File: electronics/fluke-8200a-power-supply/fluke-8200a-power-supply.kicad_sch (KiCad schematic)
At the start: 77 parts, among them J10 Conn_01x01_Socket, J11 Conn_01x01_Socket, J12 Conn_01x01_Socket, J13 Conn_01x01_Socket, J14 Conn_01x01_Socket, J2 Conn_01x01_Socket, J3 Conn_01x01_Socket, J4 Conn_01x01_Socket, J5 Conn_01x01_Socket, J6 Conn_01x01_Socket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

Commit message: PCB work.
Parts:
- C1, C10, C11, C12, C13, C3, C4, C6, C7, C8, C9: symbol Device:C -> Device:C_Polarized
- C2: value 400 -> 400uF; symbol Device:C -> Device:C_Polarized
- C5: value 125 -> 125uF; symbol Device:C -> Device:C_Polarized
- Q13: Note (none) -> Actually uses 2N3391A
- renumbered Q8 to Q10
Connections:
- net +15V: now also C3.1; no longer C3.2
- net GND: now also C1.2; no longer C1.1
- net GNDS: now also C12.2, C2.2, C3.2, C4.1; no longer C12.1, C2.1, C3.1, C4.2
- net at R5.2, R7.1: now also C12.1; no longer C12.2
- net at D2.1 (K), D4.1 (K), R1.1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: now also C1.1; no longer C1.2
- net at D5.2 (A), D7.2 (A), R16.1: now also C4.2; no longer C4.1
- net at D6.1 (K), D8.1 (K), R6.1: now also C2.1; no longer C2.2
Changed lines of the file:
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@@
   (junction (at 40.64 81.28) (diameter 0) (color 0 0 0 0)
   )
+  (junction (at 82.55 168.91) (diameter 0) (color 0 0 0 0)
+  )
+  (junction (at 167.64 73.66) (diameter 0) (color 0 0 0 0)
+  )
+  (junction (at 168.91 148.59) (diameter 0) (color 0 0 0 0)
+  )
+  (junction (at 208.28 127) (diameter 0) (color 0 0 0 0)
+  )
   (junction (at 55.88 73.66) (diameter 0) (color 0 0 0 0)
   )
-  (junction (at 82.55 168.91) (diameter 0) (color 0 0 0 0)
-  )
-  (junction (at 167.64 73.66) (diameter 0) (color 0 0 0 0)
-  )
-  (junction (at 168.91 148.59) (diameter 0) (color 0 0 0 0)
-  )
-  (junction (at 208.28 127) (diameter 0) (color 0 0 0 0)
-  )
   (junction (at 124.46 137.16) (diameter 0) (color 0 0 0 0)
   )
@@
     (stroke (width 0) (type default))
   )
+  (wire (pts (xy 55.88 73.66) (xy 62.23 73.66))
+    (stroke (width 0) (type default))
+  )
   (wire (pts (xy 205.74 109.22) (xy 205.74 101.6))
     (stroke (width 0) (type default))
@@
     (stroke (width 0) (type default))
   )
-  (wire (pts (xy 55.88 73.66) (xy 62.23 73.66))
-    (stroke (width 0) (type default))
-  )
   (wire (pts (xy 60.96 27.94) (xy 60.96 40.64))
     (stroke (width 0) (type default))
@@
     (stroke (width 0) (type default))
   )
-  (wire (pts (xy 55.88 73.66) (xy 49.53 73.66))
+  (wire (pts (xy 49.53 73.66) (xy 55.88 73.66))
     (stroke (width 0) (type default))
   )
@@
     )
   )
-  (symbol (lib_id "Device:C") (at 96.52 152.4 0) (unit 1)
+  (symbol (lib_id "Device:C_Polarized") (at 96.52 152.4 0) (unit 1)
     (in_bom yes) (on_board yes) (dnp no) (fields_autoplaced)
     (property "Reference" "C8" (at 100.33 151.13 0)
@@
     )
   )
-  (symbol (lib_id "Device:C") (at 167.64 86.36 180) (unit 1)
-    (in_bom yes) (on_board yes) (dnp no) (fields_autoplaced)
-    (property "Reference" "C3" (at 171.45 85.09 0)
-      (effects (font (size 1.27 1.27)) (justify right))
-    )
-    (property "Value" "125uF" (at 171.45 87.63 0)
-      (effects (font (size 1.27 1.27)) (justify right))
-    )
-    (property "Footprint" "Capacitor_THT:CP_Axial_L18.0mm_D8.0mm_P25.00mm_Horizontal" (at 166.6748 82.55 0)
+  (symbol (lib_id "Device:C_Polarized") (at 167.64 86.36 0) (unit 1)
+    (in_bom yes) (on_board yes) (dnp no) (fields_autoplaced)
+    (property "Reference" "C3" (at 171.45 84.201 0)
+      (effects (font (size 1.27 1.27)) (justify left))
+    )
+    (property "Value" "125uF" (at 171.45 86.741 0)
+      (effects (font (size 1.27 1.27)) (justify left))
+    )
+    (property "Footprint" "Capacitor_THT:CP_Axial_L18.0mm_D8.0mm_P25.00mm_Horizontal" (at 168.6052 90.17 0)
       (effects (font (size 1.27 1.27)) hide)
     )
@@
     )
   )
-  (symbol (lib_id "Device:C") (at 167.64 115.57 0) (unit 1)
+  (symbol (lib_id "Device:C_Polarized") (at 167.64 115.57 0) (unit 1)
     (in_bom yes) (on_board yes) (dnp no)
     (property "Reference" "C5" (at 175.26 115.57 90)
       (effects (font (size 1.27 1.27)))
     )
-    (property "Value" "125" (at 172.72 115.57 90)
+    (property "Value" "125uF" (at 172.72 115.57 90)
       (effects (font (size 1.27 1.27)))
     )
@@
     )
   )
-  (symbol (lib_id "Device:C") (at 68.58 152.4 0) (unit 1)
+  (symbol (lib_id "Device:C_Polarized") (at 68.58 152.4 0) (unit 1)
     (in_bom yes) (on_board yes) (dnp no) (fields_autoplaced)
     (property "Reference" "C6" (at 72.39 151.13 0)
@@
     )
   )
-  (symbol (lib_id "Device:C") (at 124.46 152.4 0) (unit 1)
+  (symbol (lib_id "Device:C_Polarized") (at 124.46 152.4 0) (unit 1)
     (in_bom yes) (on_board yes) (dnp no) (fields_autoplaced)
     (property "Reference" "C10" (at 128.27 151.13 0)
@@
     )
   )
-  (symbol (lib_id "Device:C") (at 60.96 48.26 180) (unit 1)
+  (symbol (lib_id "Device:C_Polarized") (at 60.96 48.26 0) (unit 1)
     (in_bom yes) (on_board yes) (dnp no) (fields_autoplaced)
     (property "Reference" "C1" (at 64.77 46.99 0)
-      (effects (font (size 1.27 1.27)) (justify right))
+      (effects (font (size 1.27 1.27)) (justify left))
     )
     (property "Value" "8uF" (at 64.77 49.53 0)
-      (effects (font (size 1.27 1.27)) (justify right))
-    )
-    (property "Footprint" "Capacitor_THT:CP_Axial_L37.0mm_D13.0mm_P43.00mm_Horizontal" (at 59.9948 44.45 0)
+      (effects (font (size 1.27 1.27)) (justify left))
+    )
+    (property "Footprint" "Capacitor_THT:CP_Axial_L37.0mm_D13.0mm_P43.00mm_Horizontal" (at 61.9252 52.07 0)
       (effects (font (size 1.27 1.27)) hide)
     )
@@
     )
   )
-  (symbol (lib_id "Device:C") (at 82.55 152.4 0) (unit 1)
+  (symbol (lib_id "Device:C_Polarized") (at 82.55 152.4 0) (unit 1)
     (in_bom yes) (on_board yes) (dnp no) (fields_autoplaced)
     (property "Reference" "C7" (at 86.36 151.13 0)
@@
     )
   )
-  (symbol (lib_id "Device:C") (at 113.03 80.01 180) (unit 1)
-    (in_bom yes) (on_board yes) (dnp no) (fields_autoplaced)
-    (property "Reference" "C12" (at 116.84 78.74 0)
-      (effects (font (size 1.27 1.27)) (justify right))
-    )
-    (property "Value" "0.047uF" (at 116.84 81.28 0)
-      (effects (font (size 1.27 1.27)) (justify right))
-    )
-    (property "Footprint" "Capacitor_THT:C_Rect_L13.0mm_W4.0mm_P10.00mm_FKS3_FKP3_MKS4" (at 112.0648 76.2 0)
+  (symbol (lib_id "Device:C_Polarized") (at 113.03 80.01 0) (unit 1)
+    (in_bom yes) (on_board yes) (dnp no) (fields_autoplaced)
+    (property "Reference" "C12" (at 116.84 77.851 0)
+      (effects (font (size 1.27 1.27)) (justify left))
+    )
+    (property "Value" "0.047uF" (at 116.84 80.391 0)
+      (effects (font (size 1.27 1.27)) (justify left))
+    )
+    (property "Footprint" "Capacitor_THT:C_Rect_L13.0mm_W4.0mm_P10.00mm_FKS3_FKP3_MKS4" (at 113.9952 83.82 0)
       (effects (font (size 1.27 1.27)) hide)
     )
@@
     )
   )
-  (symbol (lib_id "Device:C") (at 138.43 152.4 0) (unit 1)
+  (symbol (lib_id "Device:C_Polarized") (at 138.43 152.4 0) (unit 1)
     (in_bom yes) (on_board yes) (dnp no) (fields_autoplaced)
     (property "Reference" "C11" (at 142.24 151.13 0)
@@
       (effects (font (size 1.27 1.27)) (justify left) hide)
     )
+    (property "Note" "Actually uses 2N3391A" (at 163.83 163.83 0)
+      (effects (font (size 1.27 1.27)) hide)
+    )
     (pin "1")
     (pin "2")
@@
     )
   )
-  (symbol (lib_id "Device:C") (at 101.6 123.19 0) (unit 1)
+  (symbol (lib_id "Device:C_Polarized") (at 101.6 123.19 0) (unit 1)
     (in_bom yes) (on_board yes) (dnp no) (fields_autoplaced)
     (property "Reference" "C13" (at 105.41 121.92 0)
@@
     )
   )
-  (symbol (lib_id "Device:C") (at 110.49 152.4 0) (unit 1)
+  (symbol (lib_id "Device:C_Polarized") (at 110.49 152.4 0) (unit 1)
     (in_bom yes) (on_board yes) (dnp no) (fields_autoplaced)
     (property "Reference" "C9" (at 114.3 151.13 0)
@@
     )
   )
-  (symbol (lib_id "Device:C") (at 55.88 77.47 180) (unit 1)
-    (in_bom yes) (on_board yes) (dnp no) (fields_autoplaced)
-    (property "Reference" "C2" (at 59.69 76.2 0)
-      (effects (font (size 1.27 1.27)) (justify right))
-    )
-    (property "Value" "400" (at 59.69 78.74 0)
-      (effects (font (size 1.27 1.27)) (justify right))
-    )
-    (property "Footprint" "Capacitor_THT:CP_Axial_L30.0mm_D10.0mm_P35.00mm_Horizontal" (at 54.9148 73.66 0)
+  (symbol (lib_id "Device:C_Polarized") (at 55.88 77.47 0) (unit 1)
+    (in_bom yes) (on_board yes) (dnp no) (fields_autoplaced)
+    (property "Reference" "C2" (at 59.69 75.311 0)
+      (effects (font (size 1.27 1.27)) (justify left))
+    )
+    (property "Value" "400uF" (at 59.69 77.851 0)
+      (effects (font (size 1.27 1.27)) (justify left))
+    )
+    (property "Footprint" "Capacitor_THT:CP_Axial_L30.0mm_D10.0mm_P35.00mm_Horizontal" (at 56.8452 81.28 0)
       (effects (font (size 1.27 1.27)) hide)
     )
@@
     )
   )
-  (symbol (lib_id "Device:C") (at 57.15 115.57 180) (unit 1)
-    (in_bom yes) (on_board yes) (dnp no) (fields_autoplaced)
-    (property "Reference" "C4" (at 60.96 114.3 0)
-      (effects (font (size 1.27 1.27)) (justify right))
-    )
-    (property "Value" "400uF" (at 60.96 116.84 0)
-      (effects (font (size 1.27 1.27)) (justify right))
-    )
-    (property "Footprint" "Capacitor_THT:CP_Axial_L30.0mm_D10.0mm_P35.00mm_Horizontal" (at 56.1848 111.76 0)
+  (symbol (lib_id "Device:C_Polarized") (at 57.15 115.57 0) (unit 1)
+    (in_bom yes) (on_board yes) (dnp no) (fields_autoplaced)
+    (property "Reference" "C4" (at 60.96 113.411 0)
+      (effects (font (size 1.27 1.27)) (justify left))
+    )
+    (property "Value" "400uF" (at 60.96 115.951 0)
+      (effects (font (size 1.27 1.27)) (justify left))
+    )
+    (property "Footprint" "Capacitor_THT:CP_Axial_L30.0mm_D10.0mm_P35.00mm_Horizontal" (at 58.1152 119.38 0)
       (effects (font (size 1.27 1.27)) hide)
     )
@@
   (symbol (lib_id "Transistor_BJT:2N3904") (at 93.98 124.46 270) (unit 1)
     (in_bom yes) (on_board yes) (dnp no) (fields_autoplaced)
-    (property "Reference" "Q8" (at 93.98 130.81 90)
+    (property "Reference" "Q10" (at 93.98 130.81 90)
       (effects (font (size 1.27 1.27)))
     )
@@
       (project "fluke-8200a-power-supply"
         (path "/7650ab5c-233a-43dd-bf25-97d0c3dbd279"
-          (reference "Q8") (unit 1)
-        )
-      )
+          (reference "Q10") (unit 1)
+        )
+      )

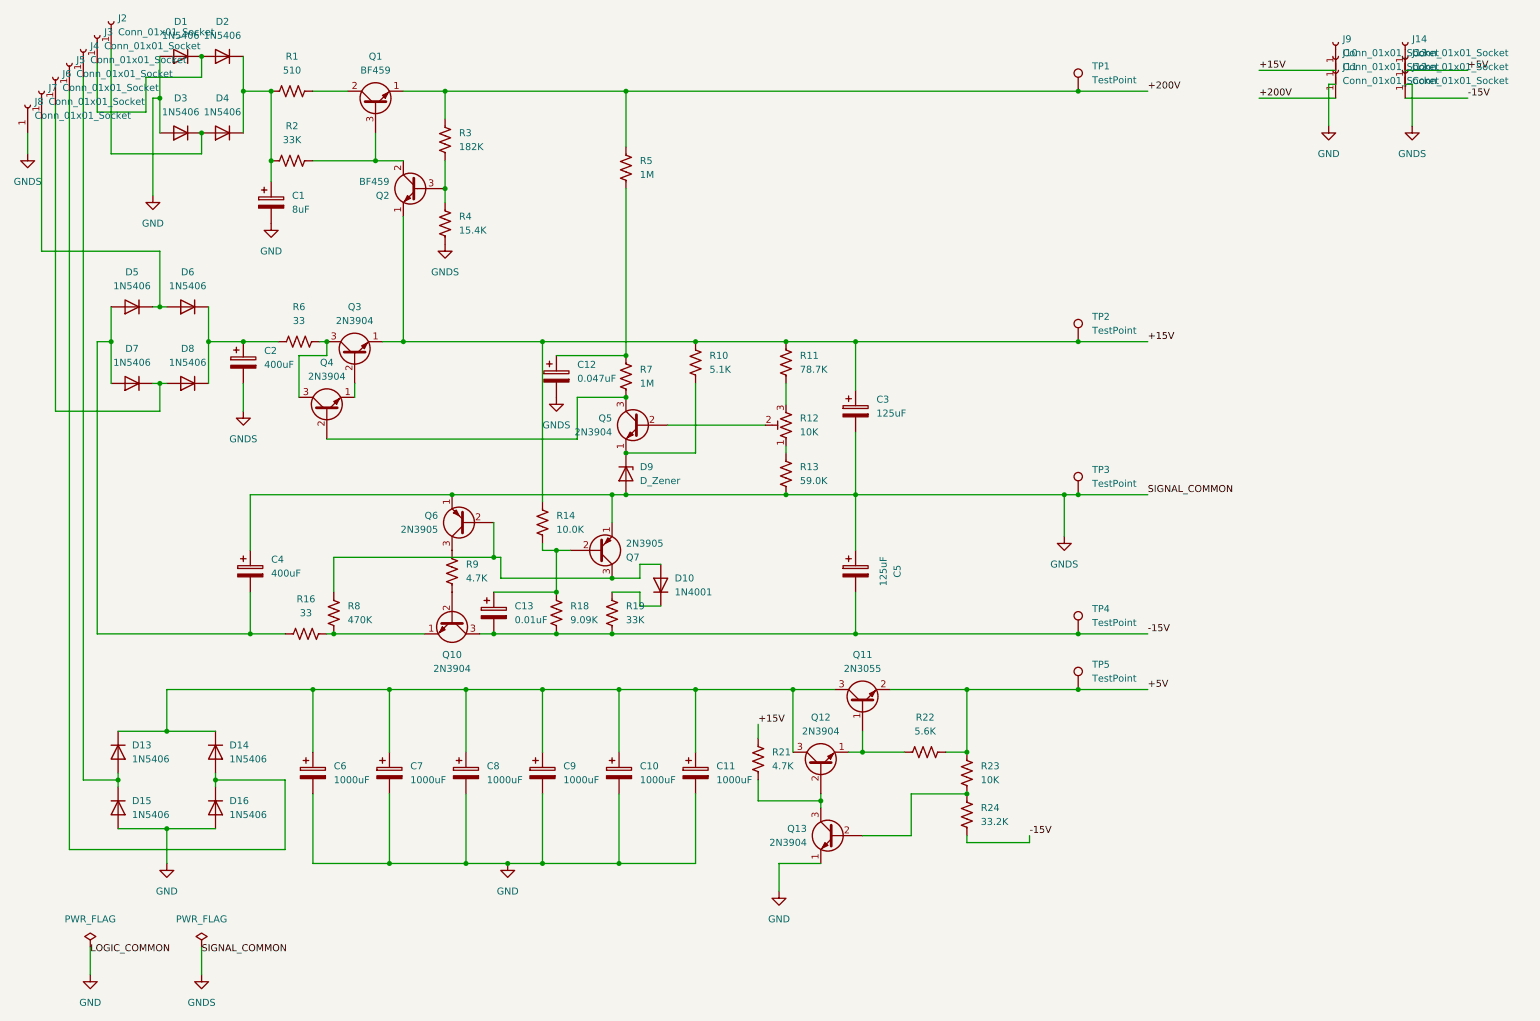
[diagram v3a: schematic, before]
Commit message: PCB quotable, but not yet fully compatable with fluke 8200A
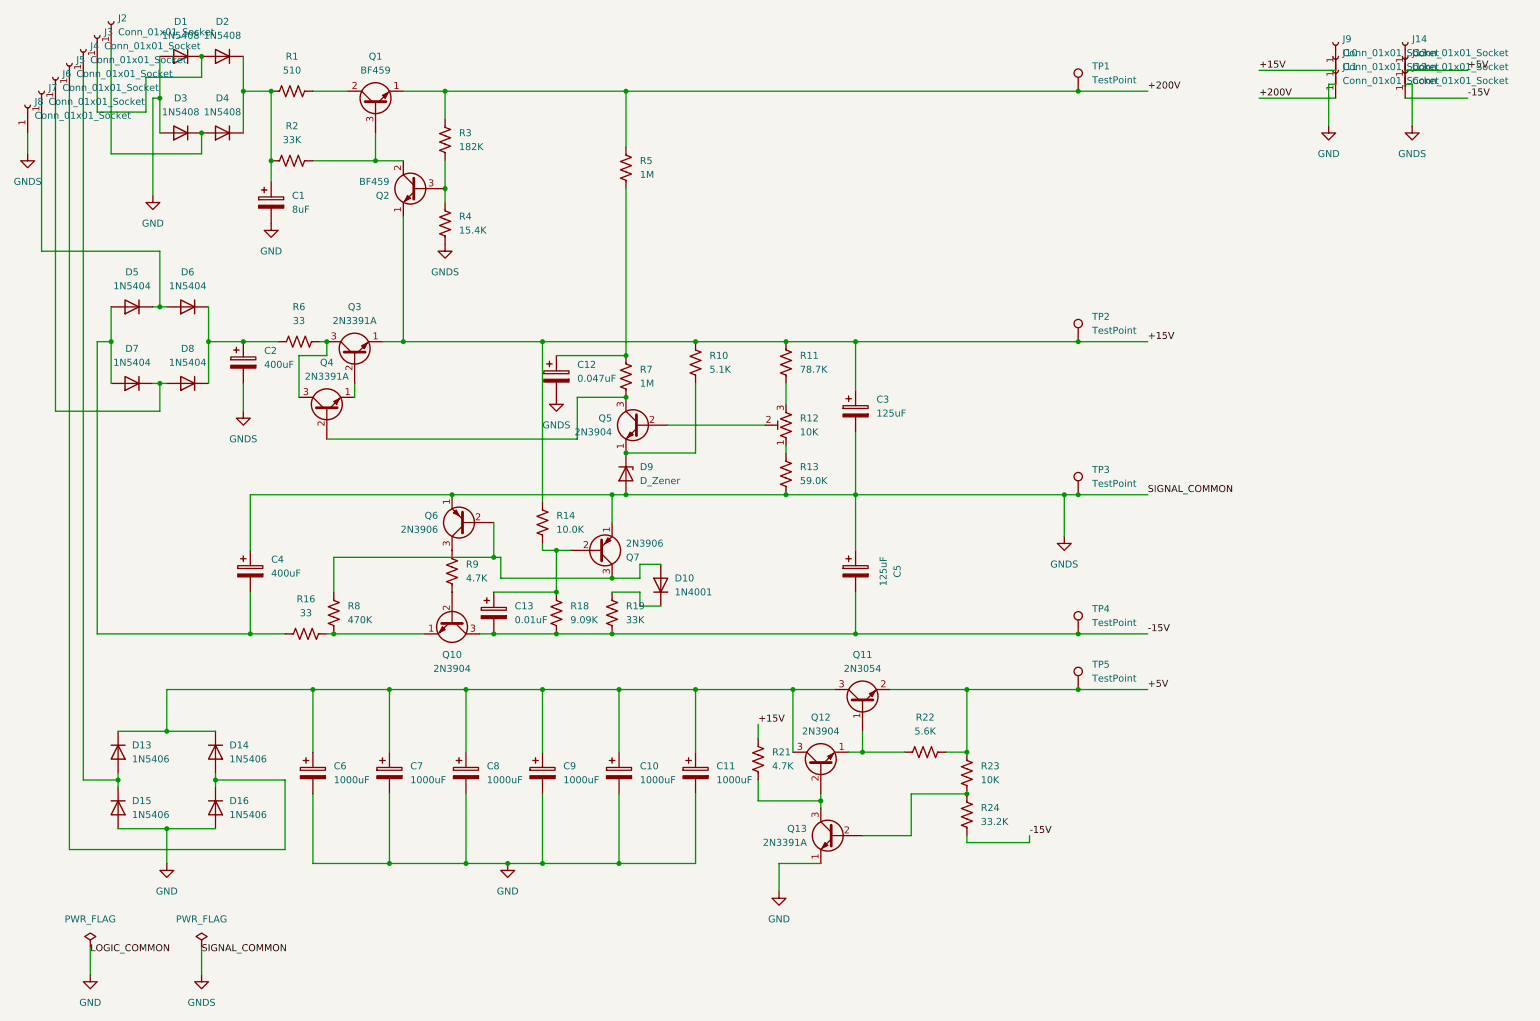
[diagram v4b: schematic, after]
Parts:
- D1, D2, D3, D4: value 1N5406 -> 1N5408; symbol Diode:1N5406 -> Diode:1N5408
- D5, D6, D7, D8: value 1N5406 -> 1N5404
- Q11: value 2N3055 -> 2N3054; footprint Package_TO_SOT_THT:TO-3 -> TO-66:TO66
- Q13, Q3, Q4: value 2N3904 -> 2N3391A
- Q6, Q7: value 2N3905 -> 2N3906
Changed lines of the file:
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@@
       (effects (font (size 1.27 1.27)))
     )
-    (property "Value" "2N3904" (at 71.12 80.01 90)
+    (property "Value" "2N3391A" (at 71.12 80.01 90)
       (effects (font (size 1.27 1.27)))
     )
@@
     )
   )
-  (symbol (lib_id "Diode:1N5406") (at 52.07 35.56 180) (unit 1)
+  (symbol (lib_id "Diode:1N5408") (at 52.07 35.56 180) (unit 1)
     (in_bom yes) (on_board yes) (dnp no) (fields_autoplaced)
     (property "Reference" "D4" (at 52.07 29.21 0)
       (effects (font (size 1.27 1.27)))
     )
-    (property "Value" "1N5406" (at 52.07 31.75 0)
+    (property "Value" "1N5408" (at 52.07 31.75 0)
       (effects (font (size 1.27 1.27)))
     )
@@
       (effects (font (size 1.27 1.27)))
     )
-    (property "Value" "1N5406" (at 35.56 63.5 0)
+    (property "Value" "1N5404" (at 35.56 63.5 0)
       (effects (font (size 1.27 1.27)))
     )
@@
     )
   )
-  (symbol (lib_id "Diode:1N5406") (at 44.45 21.59 180) (unit 1)
+  (symbol (lib_id "Diode:1N5408") (at 44.45 21.59 180) (unit 1)
     (in_bom yes) (on_board yes) (dnp no) (fields_autoplaced)
     (property "Reference" "D1" (at 44.45 15.24 0)
       (effects (font (size 1.27 1.27)))
     )
-    (property "Value" "1N5406" (at 44.45 17.78 0)
+    (property "Value" "1N5408" (at 44.45 17.78 0)
       (effects (font (size 1.27 1.27)))
     )
@@
       (effects (font (size 1.27 1.27)))
     )
-    (property "Value" "1N5406" (at 35.56 77.47 0)
+    (property "Value" "1N5404" (at 35.56 77.47 0)
       (effects (font (size 1.27 1.27)))
     )
@@
       (effects (font (size 1.27 1.27)))
     )
-    (property "Value" "1N5406" (at 45.72 63.5 0)
+    (property "Value" "1N5404" (at 45.72 63.5 0)
       (effects (font (size 1.27 1.27)))
     )
@@
     )
   )
-  (symbol (lib_id "Diode:1N5406") (at 44.45 35.56 180) (unit 1)
+  (symbol (lib_id "Diode:1N5408") (at 44.45 35.56 180) (unit 1)
     (in_bom yes) (on_board yes) (dnp no) (fields_autoplaced)
     (property "Reference" "D3" (at 44.45 29.21 0)
       (effects (font (size 1.27 1.27)))
     )
-    (property "Value" "1N5406" (at 44.45 31.75 0)
+    (property "Value" "1N5408" (at 44.45 31.75 0)
       (effects (font (size 1.27 1.27)))
     )
@@
       (effects (font (size 1.27 1.27)))
     )
-    (property "Value" "2N3904" (at 76.2 69.85 90)
+    (property "Value" "2N3391A" (at 76.2 69.85 90)
       (effects (font (size 1.27 1.27)))
     )
@@
       (effects (font (size 1.27 1.27)) (justify left))
     )
-    (property "Value" "2N3905" (at 125.73 110.49 0)
+    (property "Value" "2N3906" (at 125.73 110.49 0)
       (effects (font (size 1.27 1.27)) (justify left))
     )
@@
       (effects (font (size 1.27 1.27)) (justify left))
     )
-    (property "Value" "2N3905" (at 91.44 107.95 0)
+    (property "Value" "2N3906" (at 91.44 107.95 0)
       (effects (font (size 1.27 1.27)) (justify left))
     )
@@
     )
   )
-  (symbol (lib_id "Diode:1N5406") (at 52.07 21.59 180) (unit 1)
+  (symbol (lib_id "Diode:1N5408") (at 52.07 21.59 180) (unit 1)
     (in_bom yes) (on_board yes) (dnp no) (fields_autoplaced)
     (property "Reference" "D2" (at 52.07 15.24 0)
       (effects (font (size 1.27 1.27)))
     )
-    (property "Value" "1N5406" (at 52.07 17.78 0)
+    (property "Value" "1N5408" (at 52.07 17.78 0)
       (effects (font (size 1.27 1.27)))
     )
@@
       (effects (font (size 1.27 1.27)) (justify left))
     )
-    (property "Value" "2N3904" (at 158.75 165.1 0)
+    (property "Value" "2N3391A" (at 158.75 165.1 0)
       (effects (font (size 1.27 1.27)) (justify left))
     )
@@
       (effects (font (size 1.27 1.27)))
     )
-    (property "Value" "1N5406" (at 45.72 77.47 0)
+    (property "Value" "1N5404" (at 45.72 77.47 0)
       (effects (font (size 1.27 1.27)))
     )
@@
       (effects (font (size 1.27 1.27)))
     )
-    (property "Value" "2N3055" (at 168.91 133.35 90)
-      (effects (font (size 1.27 1.27)))
-    )
-    (property "Footprint" "Package_TO_SOT_THT:TO-3" (at 170.815 134.62 0)
+    (property "Value" "2N3054" (at 168.91 133.35 90)
+      (effects (font (size 1.27 1.27)))
+    )
+    (property "Footprint" "TO-66:TO66" (at 170.815 134.62 0)
       (effects (font (size 1.27 1.27) italic) (justify left) hide)
     )
